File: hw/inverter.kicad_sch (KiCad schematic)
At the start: 13 parts, among them J1 Conn_01x01, Q1 CSD18532Q5B, Q2 CSD18532Q5B

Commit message: basic *.kicad_sch done
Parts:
- added C25, C26, C29, C30: 3n3 X7R 100V, Capacitor_SMD:C_0603_1608Metric, symbol Device:C
- added C27, C31: 100n X7R 100V, Capacitor_SMD:C_0603_1608Metric, symbol Device:C
- added C28, C32: 4u7 X7R 100V, Capacitor_SMD:C_0603_1608Metric, symbol Device:C
- added D3, D4: D_Schottky, Package_SON:WSON-8-1EP_6x5mm_P1.27mm_EP3.4x4mm, symbol Device:D_Schottky
- added J2, J3: Conn_01x01, Connector_Wire:SolderWire-0.75sqmm_1x01_D1.25mm_OD3.5mm, symbol Connector_Generic:Conn_01x01
- added Q3, Q4, Q5, Q6: CSD18532Q5B, Package_TO_SOT_SMD:TDSON-8-1, symbol Transistor_FET:CSD18532Q5B
- added R10, R17: R_Shunt, Sensor_Humidity:Sensirion_DFN-4_1.5x1.5mm_P0.8mm_SHT4x_NoCentralPad, symbol Device:R_Shunt
- added R11, R12, R18, R19: 5R, symbol Device:R
- added R15, R16, R8, R9: 10R, symbol Device:R
- added TP16, TP17, TP18, TP19, TP20, TP21, TP22, TP23, TP24: TestPoint, TestPoint:TestPoint_Pad_D1.0mm, symbol Connector:TestPoint
- C20, C24: footprint Package_SO:SOIC-8_3.9x4.9mm_P1.27mm -> Capacitor_SMD:C_0603_1608Metric
- C21, C23: footprint Package_SO:SOIC-8_3.9x4.9mm_P1.27mm -> Capacitor_SMD:C_0603_1608Metric; now not fitted
- R5, R6: now not fitted
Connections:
- net +VBAT: now also C27.1, C28.1, C31.1, C32.1, Q3.5 (D), Q5.5 (D), R11.2, R18.2
- net GHA: now also TP16.1
- net GLA: now also TP18.1
- net GND: now also C28.2, C32.2, D3.2 (A), D4.2 (A), R10.1, R17.1
- net SHA: now also TP17.1
- net SNUBH_A: now also C25.1, C29.1, R11.1, R18.1
- net SNUBL_A: now also C26.2, C30.2, R12.2, R19.2
- new net: C27.2, Q4.1 (S), Q4.2 (S), Q4.3 (S), R10.4, R12.1
- new net: Q3.4 (G), R8.2
- new net: Q5.4 (G), R15.2
- new net: C31.2, Q6.1 (S), Q6.2 (S), Q6.3 (S), R17.4, R19.1
- new net: D4.1 (K), Q6.4 (G), R16.2
- new net: D3.1 (K), Q4.4 (G), R9.2
- new net GHB: R8.1, TP19.1
- new net GHC: R15.1, TP22.1, TP24.1
- new net GLB: R9.1, TP21.1
- new net GLC: R16.1
- new net SHB: C25.2, C26.1, J2.1 (Pin_1), Q3.1 (S), Q3.2 (S), Q3.3 (S), Q4.5 (D), TP20.1
- new net SHC: C29.2, C30.1, J3.1 (Pin_1), Q5.1 (S), Q5.2 (S), Q5.3 (S), Q6.5 (D), TP23.1
- new net SNB: R10.2
- new net SNC: R17.2
- new net SPB: R10.3
- new net SPC: R17.3
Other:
- moved on the sheet: C24

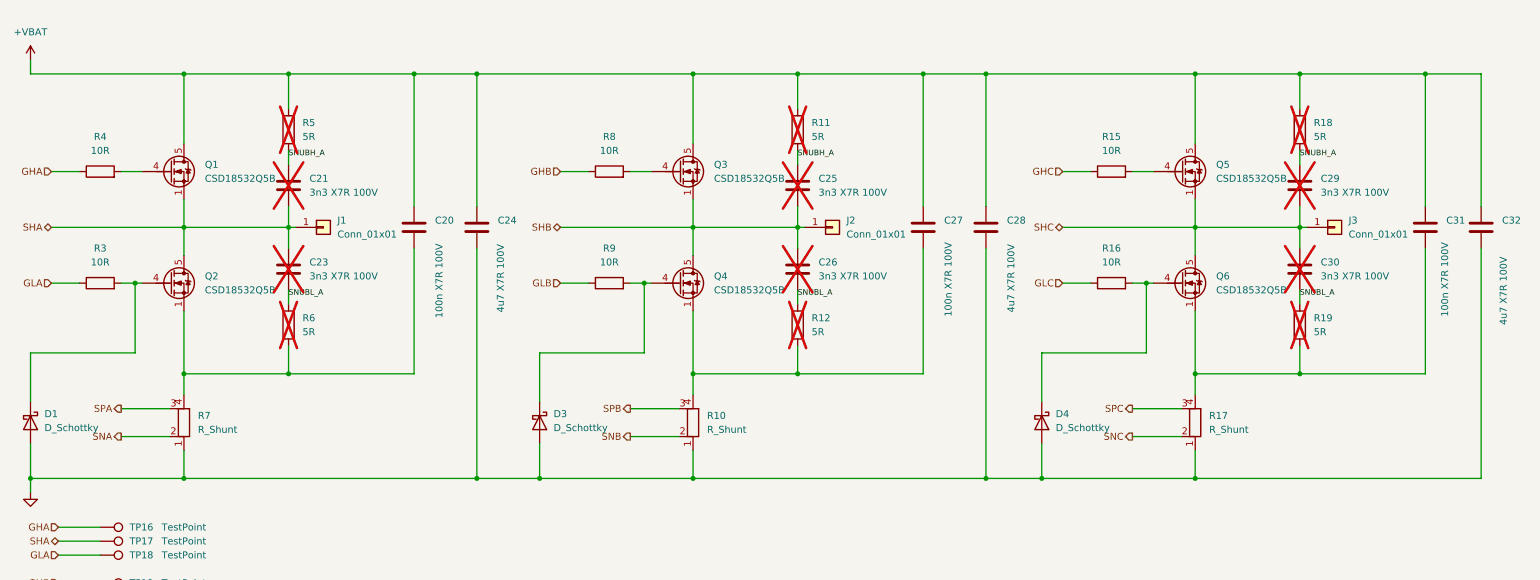
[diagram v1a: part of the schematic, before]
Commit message: began with lcsc and footprints
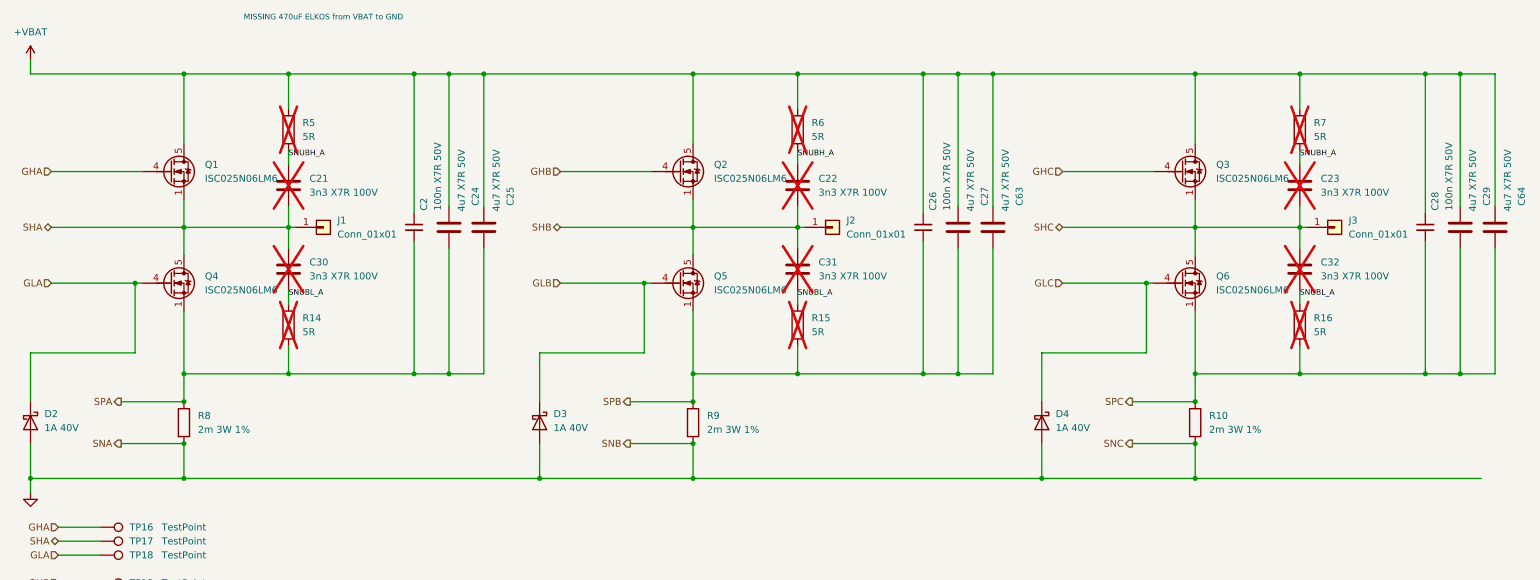
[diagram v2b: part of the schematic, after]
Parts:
- removed C20, C31: 100n X7R 100V, Capacitor_SMD:C_0603_1608Metric, symbol Device:C
- removed C28, C32: 4u7 X7R 100V, Capacitor_SMD:C_0603_1608Metric, symbol Device:C
- removed D1: D_Schottky, Package_SON:WSON-8-1EP_6x5mm_P1.27mm_EP3.4x4mm, symbol Device:D_Schottky
- removed R10, R17, R7: R_Shunt, Sensor_Humidity:Sensirion_DFN-4_1.5x1.5mm_P0.8mm_SHT4x_NoCentralPad, symbol Device:R_Shunt
- removed R15, R16, R3, R4: 10R, symbol Device:R
- added C2, C26, C28: 100n X7R 50V, Capacitor_SMD:C_0603_1608Metric, symbol Device:C_Small
- added C25, C29, C63, C64: 4u7 X7R 50V, Capacitor_SMD:C_1206_3216Metric, symbol Device:C
- added D2: 1A 40V, Diode_SMD:D_SOD-123, symbol Device:D_Schottky
- added R10: 2m 3W 1%, Resistor_SMD:R_2512_6332Metric, symbol Device:R
- C24: value 4u7 X7R 100V -> 4u7 X7R 50V; footprint Capacitor_SMD:C_0603_1608Metric -> Capacitor_SMD:C_1206_3216Metric; LCSC (none) -> C29823
- C27: value 100n X7R 100V -> 4u7 X7R 50V; footprint Capacitor_SMD:C_0603_1608Metric -> Capacitor_SMD:C_1206_3216Metric; LCSC (none) -> C29823
- D3, D4: value D_Schottky -> 1A 40V; footprint Package_SON:WSON-8-1EP_6x5mm_P1.27mm_EP3.4x4mm -> Diode_SMD:D_SOD-123; LCSC (none) -> C8598
- J1: footprint Connector_Wire:SolderWire-0.75sqmm_1x01_D1.25mm_OD3.5mm -> Connector_Wire:SolderWire-6sqmm_1x01_D3.5mm_OD7mm
- Q1, Q2, Q3, Q4, Q5, Q6: value CSD18532Q5B -> ISC025N06LM6
- R8, R9: value 10R -> 2m 3W 1%; footprint (none) -> Resistor_SMD:R_2512_6332Metric; LCSC (none) -> C7420017
- renumbered C25 to C22, C29 to C23, C23 to C30, C26 to C31, C30 to C32, R6 to R14, R12 to R15, R19 to R16, R11 to R6, R18 to R7
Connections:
- net +VBAT: now also Q2.5 (D), C2.1, C25.1, C26.1, C28.1, C29.1, C63.1, C64.1; no longer Q5.5 (D)
- net GHA: now also Q1.4 (G)
- net GHB: now also Q2.4 (G); no longer R8.1
- net GHC: now also Q3.4 (G)
- net GLA: now also Q4.4 (G), D2.1 (K)
- net GLB: now also D3.1 (K), Q5.4 (G); no longer R9.1
- net GLC: now also D4.1 (K), Q6.4 (G)
- net GND: now also R8.2, R9.2, D2.2 (A), R10.2; no longer C24.2
- net SHA: now also Q4.5 (D); no longer Q2.5 (D)
- net SHB: now also Q2.1 (S), Q2.2 (S), Q2.3 (S), Q5.5 (D); no longer Q3.1 (S), Q3.2 (S), Q3.3 (S), Q4.5 (D)
- net SHC: now also Q3.1 (S), Q3.2 (S), Q3.3 (S); no longer Q5.1 (S), Q5.2 (S), Q5.3 (S)
- net SPA: now also C24.2, Q4.1 (S), Q4.2 (S), Q4.3 (S), R14.1, R8.1, C2.2, C25.2
- net SPB: now also C27.2, Q5.1 (S), Q5.2 (S), Q5.3 (S), R15.1, R9.1, C26.2, C63.2
- net SPC: now also Q6.1 (S), Q6.2 (S), Q6.3 (S), R16.1, C28.2, C29.2, C64.2, R10.1
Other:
- note added: "MISSING 470uF ELKOS from VBAT to GND"

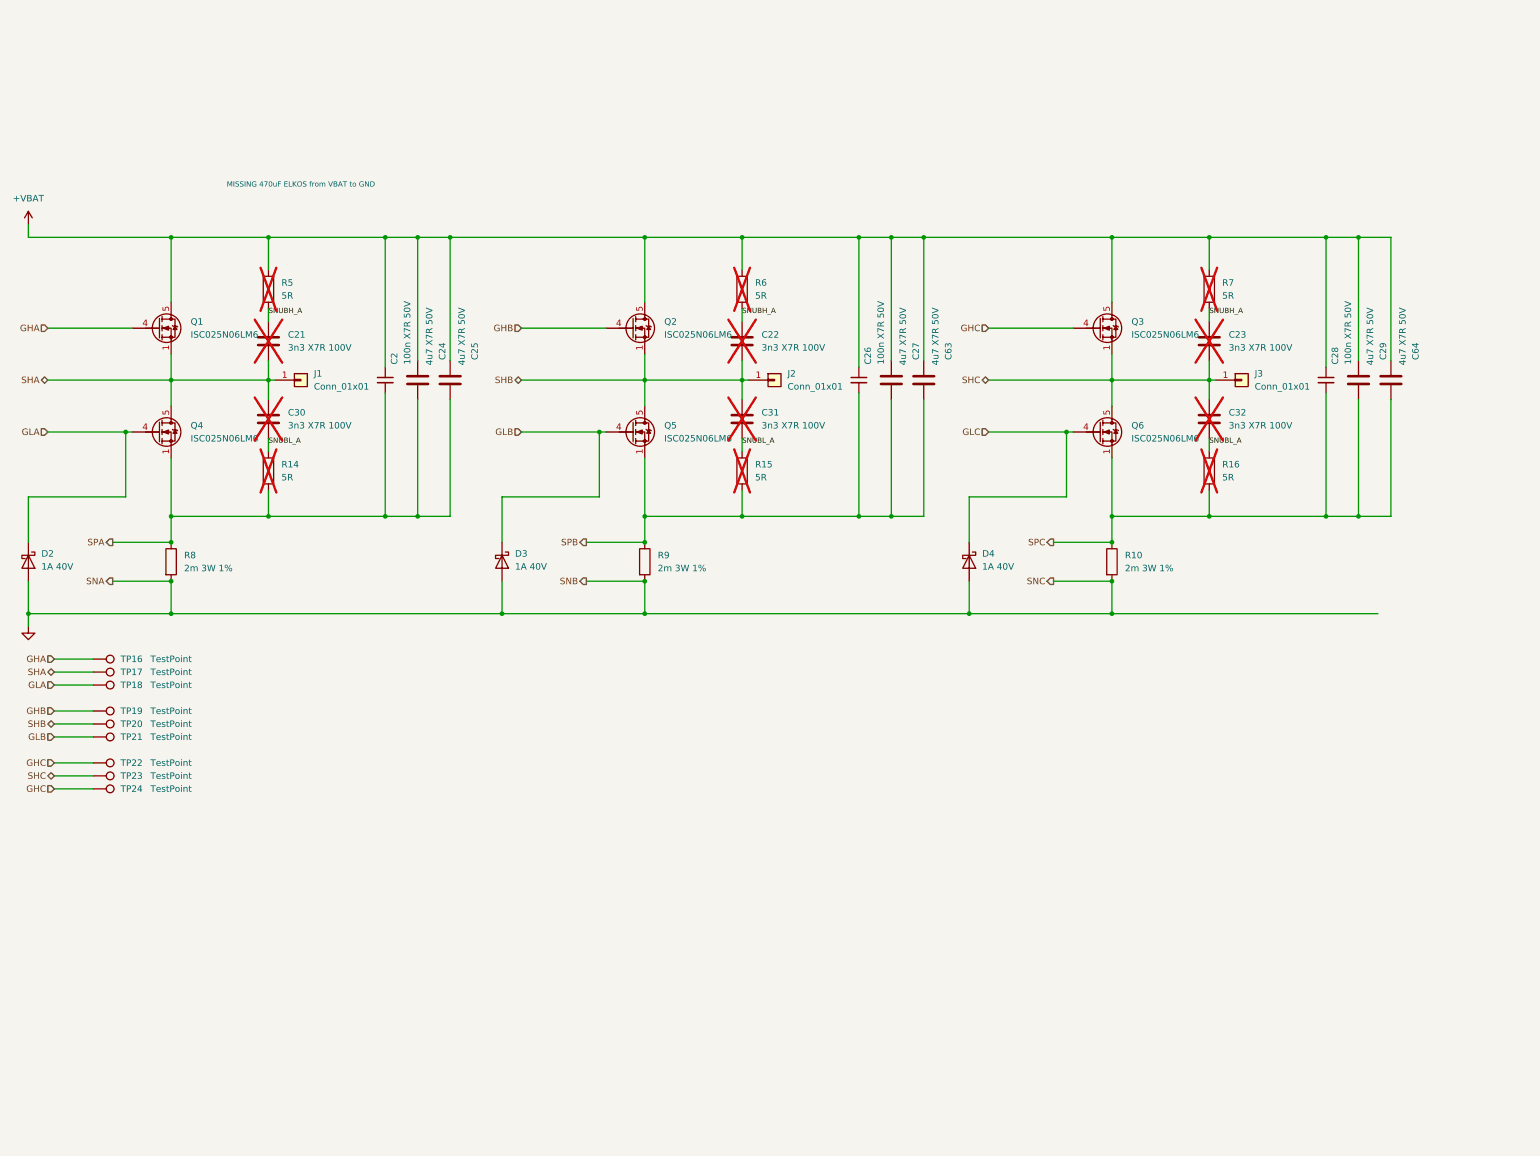
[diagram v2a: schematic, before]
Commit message: cleaned up *.kicad_sch
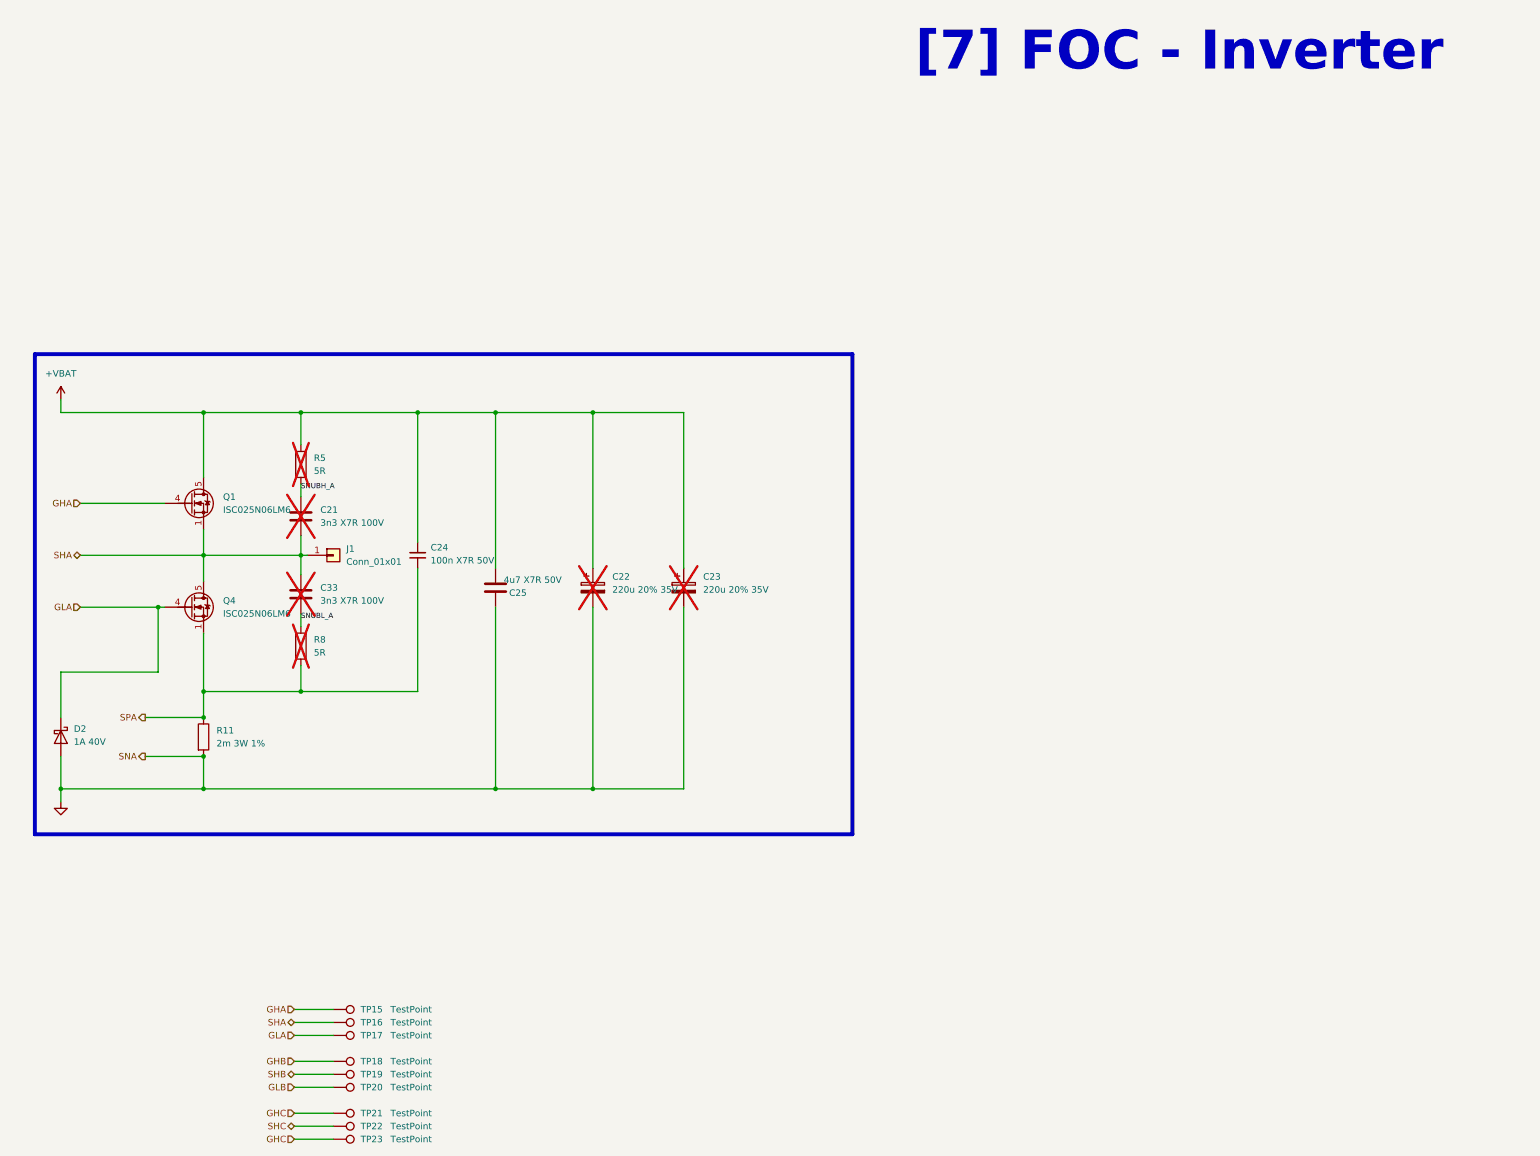
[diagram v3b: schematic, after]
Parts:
- removed C22, C23, C31, C32: 3n3 X7R 100V, Capacitor_SMD:C_0603_1608Metric, symbol Device:C
- removed C25, C27, C29, C63, C64: 4u7 X7R 50V, Capacitor_SMD:C_1206_3216Metric, symbol Device:C
- removed C26, C28: 100n X7R 50V, Capacitor_SMD:C_0603_1608Metric, symbol Device:C_Small
- removed D3, D4: 1A 40V, Diode_SMD:D_SOD-123, symbol Device:D_Schottky
- removed J2, J3: Conn_01x01, Connector_Wire:SolderWire-0.75sqmm_1x01_D1.25mm_OD3.5mm, symbol Connector_Generic:Conn_01x01
- removed Q2, Q3, Q5, Q6: ISC025N06LM6, Package_TO_SOT_SMD:TDSON-8-1, symbol Transistor_FET:CSD18532Q5B
- removed R10, R9: 2m 3W 1%, Resistor_SMD:R_2512_6332Metric, symbol Device:R
- removed R15, R16, R6, R7: 5R, symbol Device:R
- added C22, C23: 220u 20% 35V, Capacitor_SMD:CP_Elec_8x10.5, symbol Device:C_Polarized
- J1: footprint Connector_Wire:SolderWire-6sqmm_1x01_D3.5mm_OD7mm -> A_pad:Goated holy pad
- renumbered C2 to C24, C24 to C25, C30 to C33, R8 to R11, R14 to R8, TP16 to TP15, TP17 to TP16, TP18 to TP17, TP19 to TP18, TP20 to TP19, TP21 to TP20, TP22 to TP21, TP23 to TP22, TP24 to TP23
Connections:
- net +VBAT: now also C22.1, C23.1
- net GND: now also C25.2, C22.2, C23.2
- net SPA: no longer C25.2
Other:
- note added: "[7] FOC - Inverter"
- note removed: "MISSING 470uF ELKOS from VBAT to GND"
- moved on the sheet: C21, C24, C25, C33, D2, J1, Q1, Q4, R11, R5, R8, TP15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
